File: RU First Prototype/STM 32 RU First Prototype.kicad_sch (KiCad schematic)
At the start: 91 parts, among them J1 Conn_01x02, J10 Conn_01x02_Pin, J11 Conn_01x02_Pin, J12 1776113-2, J2 USB_C_Receptacle, J3 Conn_01x02_Pin, J4 Conn_01x04, J5 Conn_01x02_Pin, J7 1776113-2, J9 Conn_01x02_Pin, Q1 SISA96DN-T1, Q3 SISA96DN-T1, SW1 SW_SPDT, U1 STM32F412RGTx, U2 AMS1117-3.3, U3 MS5611, U4 KX134-1211, U5 W25Q16JVSS, U6 TCAN330, U7 TCAN330, Y1 Crystal_8Mhz

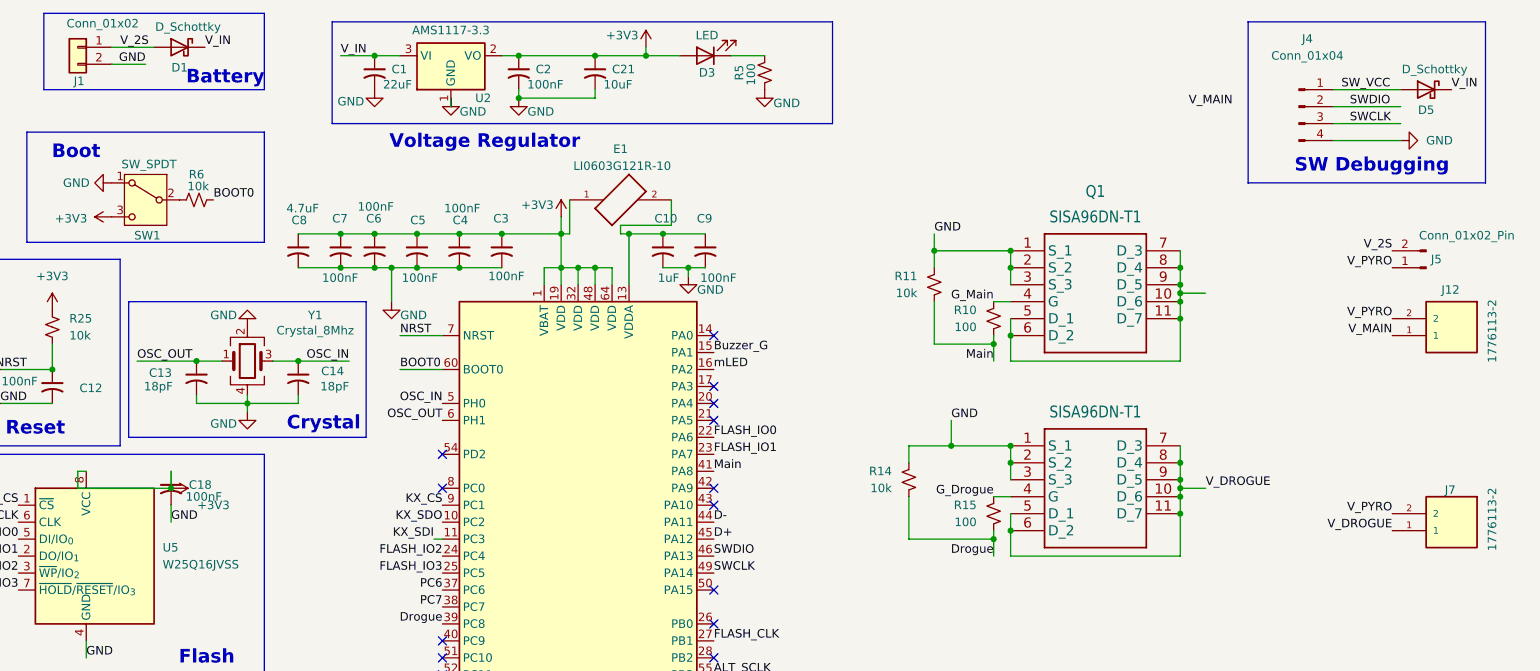
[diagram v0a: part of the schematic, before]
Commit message: Edge cuts to start
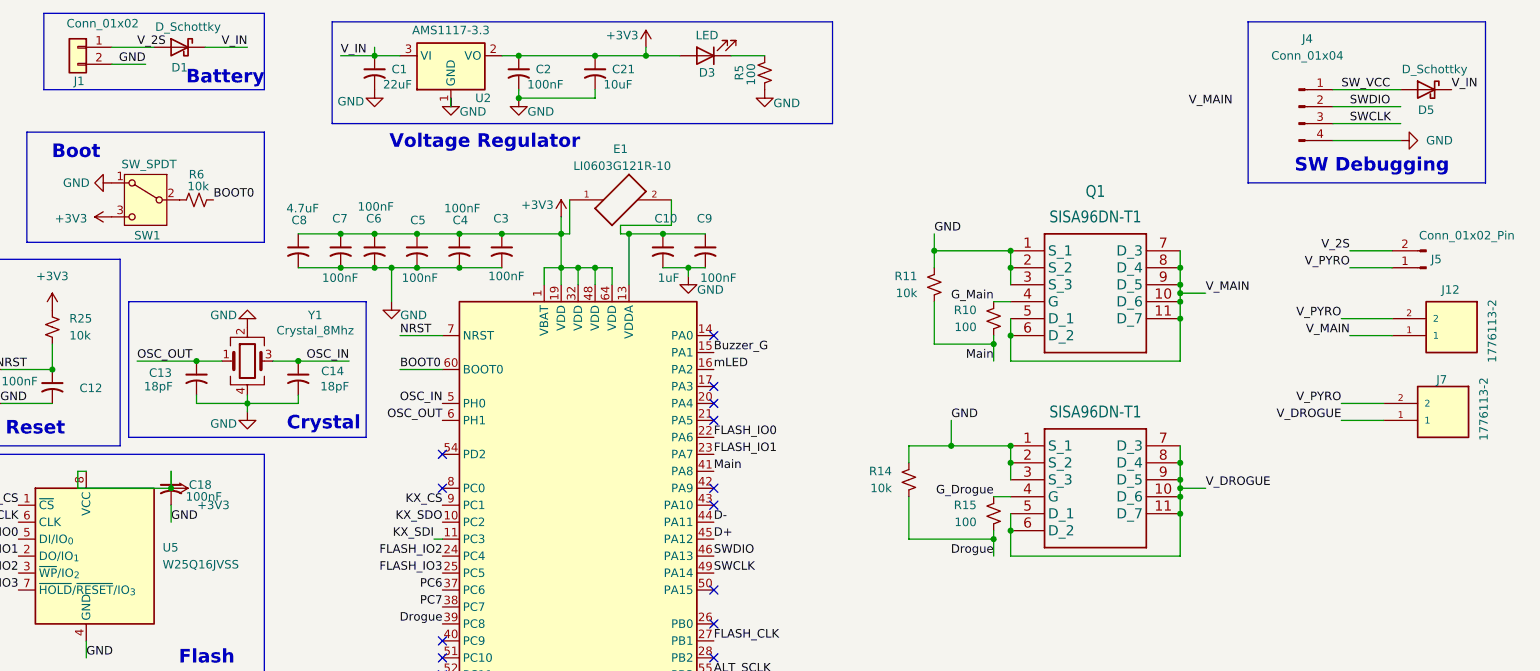
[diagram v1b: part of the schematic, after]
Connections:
- net V_MAIN: now also Q1.10 (D_6), Q1.11 (D_7), Q1.5 (D_1), Q1.6 (D_2), Q1.7 (D_3), Q1.8 (D_4), Q1.9 (D_5)
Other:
- moved on the sheet: J7
